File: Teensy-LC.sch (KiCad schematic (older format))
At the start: 37 parts, among them J202 Conn_01x03_Female, J203 I2C_BUS, Q201 SSM3K329R, Q202 SSM3K329R, Q203 SSM3J334R, SW201 SW_Up, SW202 SW_Down, SW203 SW_Enter, U201 LCD 2004A Right Angle Header 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, U202 Teensy-LC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

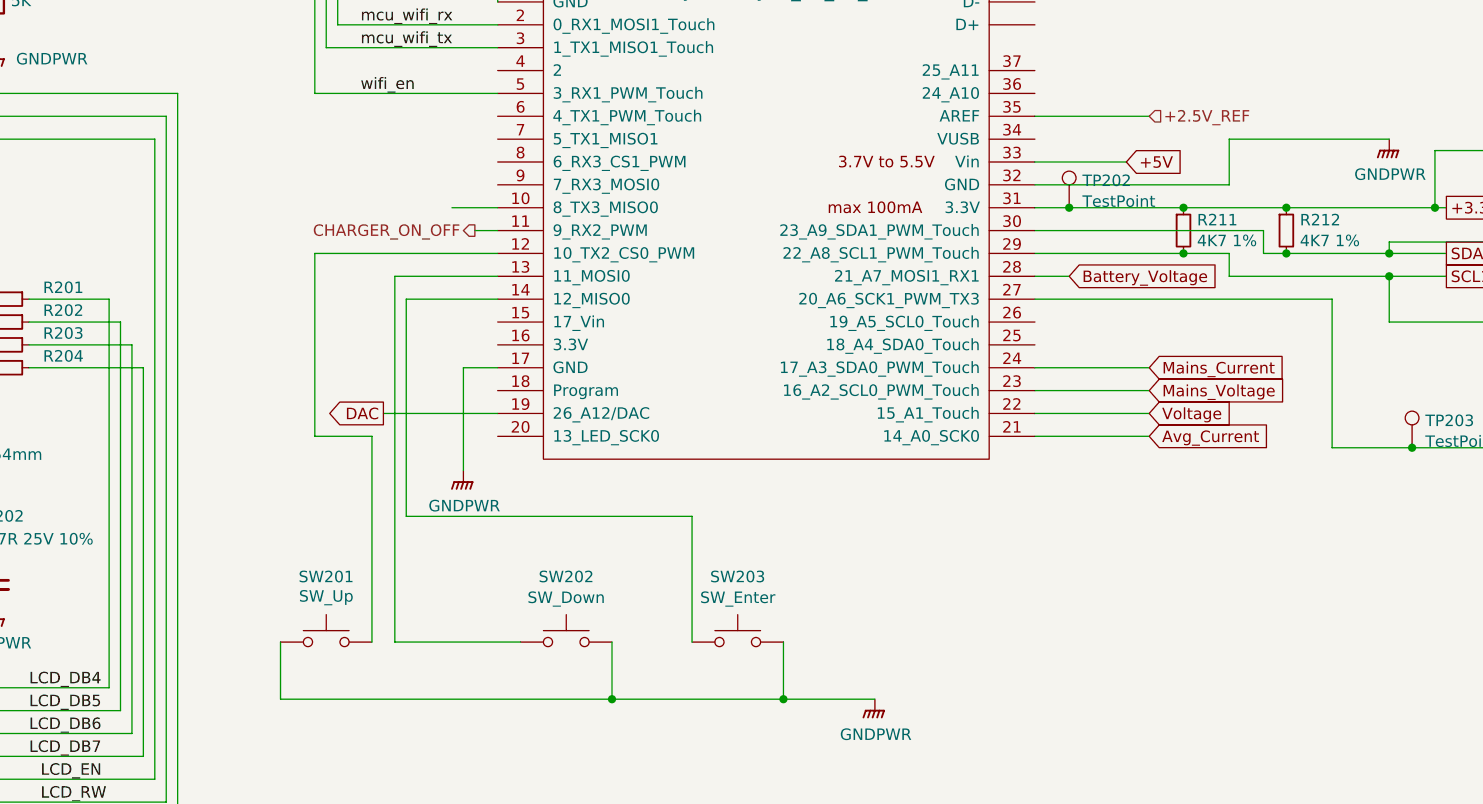
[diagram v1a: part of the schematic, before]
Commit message: Added voltage divider network and input protection to measure, the Solar input voltage, I decided this would be usefull in the cases where the solar is producing voltage over 160V, but the house is stillimporting power from the Grid, there is not point in powering up the boost converter because we can't get power into the system, as output is 160V.  Also update the TestPoint footprints to match the latest Kicad naming convention, simular to my resistor and capacitor footprint changes a few commits ago.
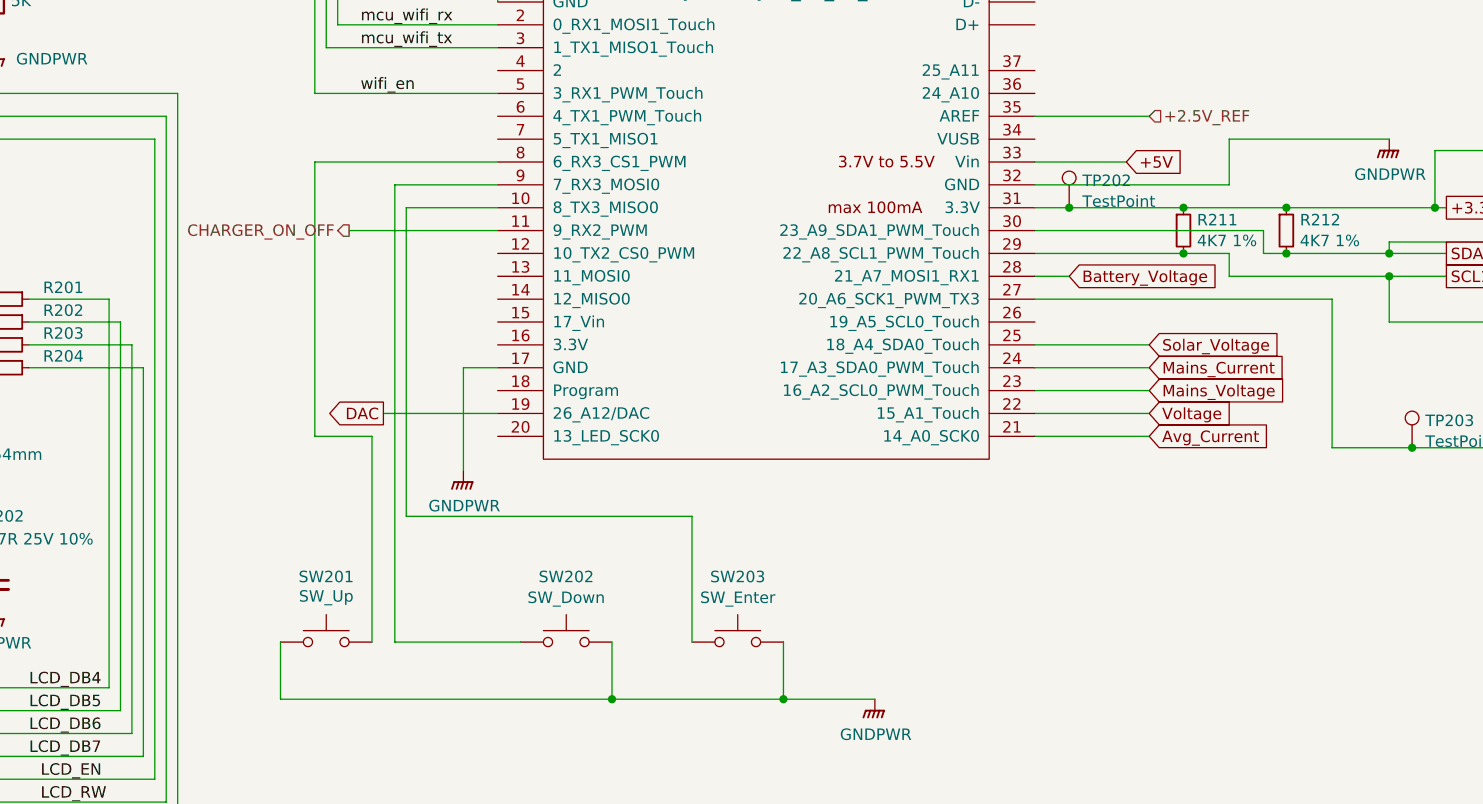
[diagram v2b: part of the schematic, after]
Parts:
- TP201, TP202, TP203: footprint Measurement_Points:Measurement_Point_Square-SMD-Pad_Big -> TestPoint:TestPoint_Pad_3.0x3.0mm
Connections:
- net at U202.10 (8_TX3_MISO0): now also SW203.1
- net at U202.12 (10_TX2_CS0_PWM): no longer SW201.2
- net at U202.13 (11_MOSI0): no longer SW202.1
- net at U202.14 (12_MISO0): no longer SW203.1
- net Solar_Voltage: now reaches U202.25 (18_A4_SDA0_Touch)
- net at U202.8 (6_RX3_CS1_PWM): now also SW201.2
- net at U202.9 (7_RX3_MOSI0): now also SW202.1
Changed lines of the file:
@@
 F 0 "TP201" H 1208 4518 50  0000 L CNN
 F 1 "TestPoint" H 1208 4427 50  0000 L CNN
-F 2 "Measurement_Points:Measurement_Point_Square-SMD-Pad_Big" H 1350 4400 50  0001 C CNN
+F 2 "TestPoint:TestPoint_Pad_3.0x3.0mm" H 1350 4400 50  0001 C CNN
 F 3 "~" H 1350 4400 50  0001 C CNN
 F 4 "-" H 0   0   50  0001 C CNN "MFR"
@@
 F 0 "TP202" H 7758 4568 50  0000 L CNN
 F 1 "TestPoint" H 7758 4477 50  0000 L CNN
-F 2 "Measurement_Points:Measurement_Point_Square-SMD-Pad_Big" H 7900 4450 50  0001 C CNN
+F 2 "TestPoint:TestPoint_Pad_3.0x3.0mm" H 7900 4450 50  0001 C CNN
 F 3 "~" H 7900 4450 50  0001 C CNN
 F 4 "-" H 0   0   50  0001 C CNN "MFR"
@@
 F 0 "TP203" H 9258 5618 50  0000 L CNN
 F 1 "TestPoint" H 9258 5527 50  0000 L CNN
-F 2 "Measurement_Points:Measurement_Point_Square-SMD-Pad_Big" H 9400 5500 50  0001 C CNN
+F 2 "TestPoint:TestPoint_Pad_3.0x3.0mm" H 9400 5500 50  0001 C CNN
 F 3 "~" H 9400 5500 50  0001 C CNN
 F 4 "-" H 1500 650 50  0001 C CNN "MFR"
@@
 Text GLabel 2400 2350 1    50   Input ~ 0
 +5V
-Text HLabel 5100 4550 0    50   Output ~ 0
+Text HLabel 4550 4550 0    50   Output ~ 0
 CHARGER_ON_OFF
 Text HLabel 9850 5500 2    50   Output ~ 0
@@
 	5200 3150 5000 3150
 Wire Wire Line
-	5200 4550 5100 4550
+	5200 4550 4550 4550
 Wire Wire Line
 	8050 4050 7550 4050
@@
 	6050 5800 4800 5800
 Wire Wire Line
-	4800 5800 4800 4850
-Wire Wire Line
-	4800 4850 5200 4850
-Wire Wire Line
 	5300 6350 4750 6350
 Wire Wire Line
@@
 	1450 6650 1900 6650
 Wire Wire Line
-	5200 4450 5000 4450
-Wire Wire Line
 	8050 5150 7550 5150
 Wire Wire Line
@@
 	10300 4050 10300 5000
 Wire Wire Line
-	4750 4750 4750 6350
-Wire Wire Line
-	4750 4750 5200 4750
-Wire Wire Line
 	8650 4650 9100 4650
 Wire Wire Line
@@
 Wire Wire Line
 	4650 5450 4400 5450
-Wire Wire Line
-	4400 5450 4400 4650
-Wire Wire Line
-	4400 4650 5200 4650
 Wire Wire Line
 	2400 2350 2400 2500
@@
 Connection ~ 9200 5500
 Connection ~ 8200 4650
+Wire Wire Line
+	4400 4250 5200 4250
+Wire Wire Line
+	4400 4250 4400 5450
+Wire Wire Line
+	4750 4350 5200 4350
+Wire Wire Line
+	4750 4350 4750 6350
+Wire Wire Line
+	4800 4450 4800 5800
+Wire Wire Line
+	4800 4450 5200 4450
+Text GLabel 8050 5050 2    50   Input ~ 0
+Solar_Voltage
+Wire Wire Line
+	8050 5050 7550 5050
 $EndSCHEMATC

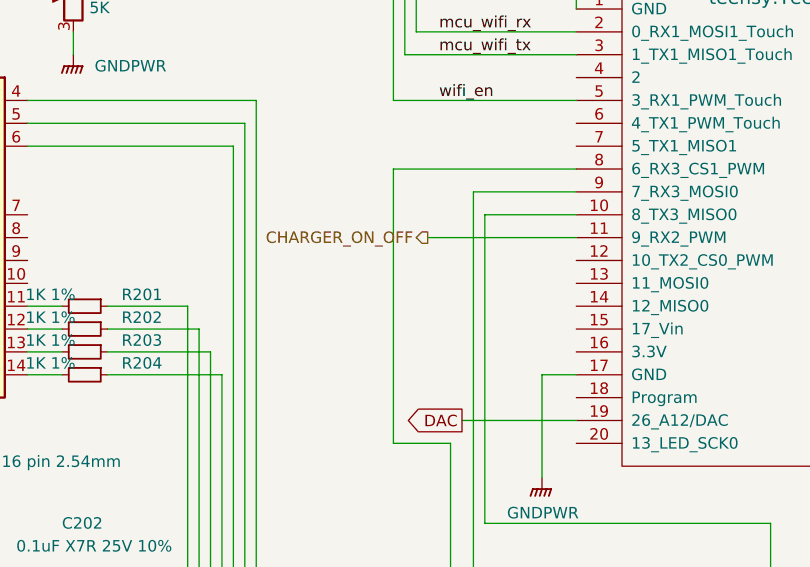
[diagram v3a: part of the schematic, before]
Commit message: Added Current_Range_Hi_Lo signal from the Mains Current Sense circuit to the Micro so we can tell what range we are operating on.
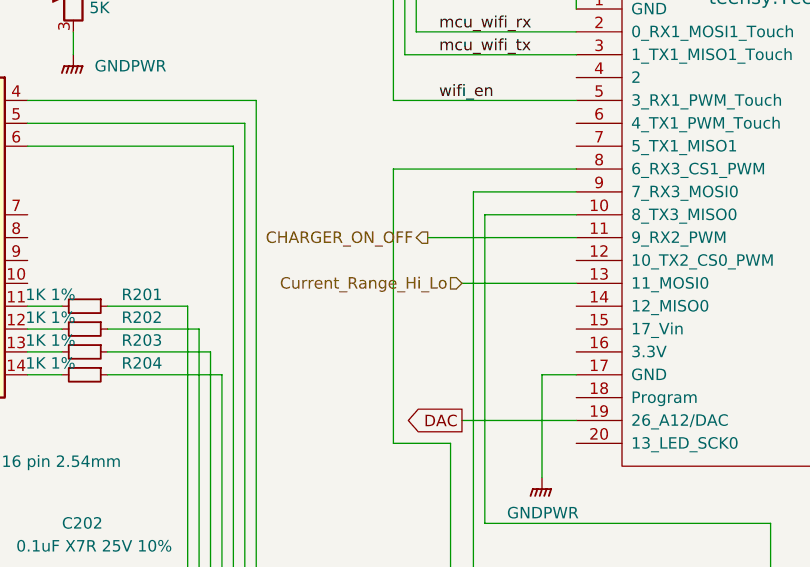
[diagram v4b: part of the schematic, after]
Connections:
- net Current_Range_Hi_Lo: now reaches U202.13 (11_MOSI0)
